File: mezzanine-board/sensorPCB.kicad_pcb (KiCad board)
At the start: 2 copper layers, 50 x 8 mm, 22 parts, among them J1 SFMC-105-01-L-D, U1 AS72651, U2 4MB Flash, U3 AS72652, U4 AS72653

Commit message: Fixed warnings
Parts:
- D1: footprint LED_SMD:LED_01005_0402Metric -> LED_SMD:LED_0603_1608Metric
- moved D1 0.68 mm to (130.9, 88.1)
- moved R6 0.64 mm to (98.9, 92.2)

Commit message: Initial Routing
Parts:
- C1, C2, C3, C4, C5, C6, C7, R4, R5, R6, R7, U2: moved to F.Cu
- moved C7 29.4 mm to (125.3, 84.6)
- moved C2 16.4 mm to (121.7, 87.0)
- moved C1 16.1 mm to (119.4, 84.6), turned to 0 degrees
- moved U2 14.7 mm to (129.9, 85.7)
- moved R7 13.8 mm to (112.6, 93.0)
- moved C5 11.8 mm to (110.2, 84.5), turned to 0 degrees
- moved C3 10.7 mm to (112.8, 86.7)
- moved R3 8.96 mm to (121.2, 92.7)
- moved R5 8.68 mm to (97.2, 84.5), turned to 0 degrees
- moved D1 8.64 mm to (123.1, 84.6)
- moved R4 8.41 mm to (116.1, 84.6), turned to 0 degrees
- moved R1 8.29 mm to (112.9, 90.0), turned to 90 degrees
- moved C6 6.35 mm to (103.8, 86.9)
- moved R2 6.06 mm to (121.7, 90.3), turned to 90 degrees
- moved R6 5.24 mm to (103.8, 90.2), turned to 90 degrees
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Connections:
- J1 pad 1: SPI_MOSI -> CSN_EE
- J1 pad 10: INT -> GND
- J1 pad 2: SPI_SCK -> RX/SCL
- J1 pad 4: RESN -> TX/SDA
- J1 pad 5: CSN_EE -> SPI_MOSI
- J1 pad 6: GND -> INT
- J1 pad 7: RX/SCL -> SPI_SCK
- J1 pad 9: TX/SDA -> RESN
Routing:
- net SPI_MOSI: track 19.2 -> 40.7 mm, vias 2 -> 1
- net +3.3V: track 106.6 -> 87.0 mm, vias 9 -> 11
- net GND: track 55.3 -> 71.2 mm, vias 5 -> 7
- net SPI_SCK: track 26.2 -> 39.8 mm
- net TX/SDA: track 20.4 -> 8.05 mm
- net I2C_ENA: track 17.2 -> 6.60 mm
- net Net-(D1-A): track 15.0 -> 5.39 mm, vias 2 -> 0
- net RESN: track 21.7 -> 30.4 mm
- net CSN_EE: track 18.2 -> 26.6 mm, vias 2 -> 1
- net SPI_MISO: track 23.1 -> 31.4 mm, vias 3 -> 1
- net RX/SCL: track 13.8 -> 6.43 mm
- net INT: track 35.4 -> 28.7 mm, vias 5 -> 3
- net /SLV1_RESN: track 25.7 -> 32.1 mm, vias 1 -> 0
- net /SCL: track 26.9 -> 29.0 mm, vias 2 -> 4
- net /SLV2_RESN: track 4.36 -> 2.49 mm, vias 1 -> 0
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- added copper zone on B.Cu, net GND
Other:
- board size 50 x 8 mm -> 50 x 12.5 mm

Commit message: Update larger board design
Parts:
- H1, H2: footprint Mounting_Wuerth:Mounting_Wuerth_WA-SMSI-M2.5_H0.5mm_9774005151 -> MountingHole:MountingHole_2.7mm_M2.5
- moved H2 0.70 mm to (136.0, 91.0)
- moved H1 0.31 mm to (92.0, 91.0)
- moved J1 0.17 mm to (124.4, 91.7)
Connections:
- U1 pad 15: Net-(D1-A) -> unconnected-(U1-LED_DRV-Pad15)
- U1 pad 18: unconnected-(U1-LED_IND-Pad18) -> Net-(D1-A)
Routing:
- net Net-(D1-A): track 5.39 -> 6.14 mm, vias 0 -> 2
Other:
- board size 50 x 12.5 mm -> 51 x 13 mm
- board text added: "DNP for I2C"

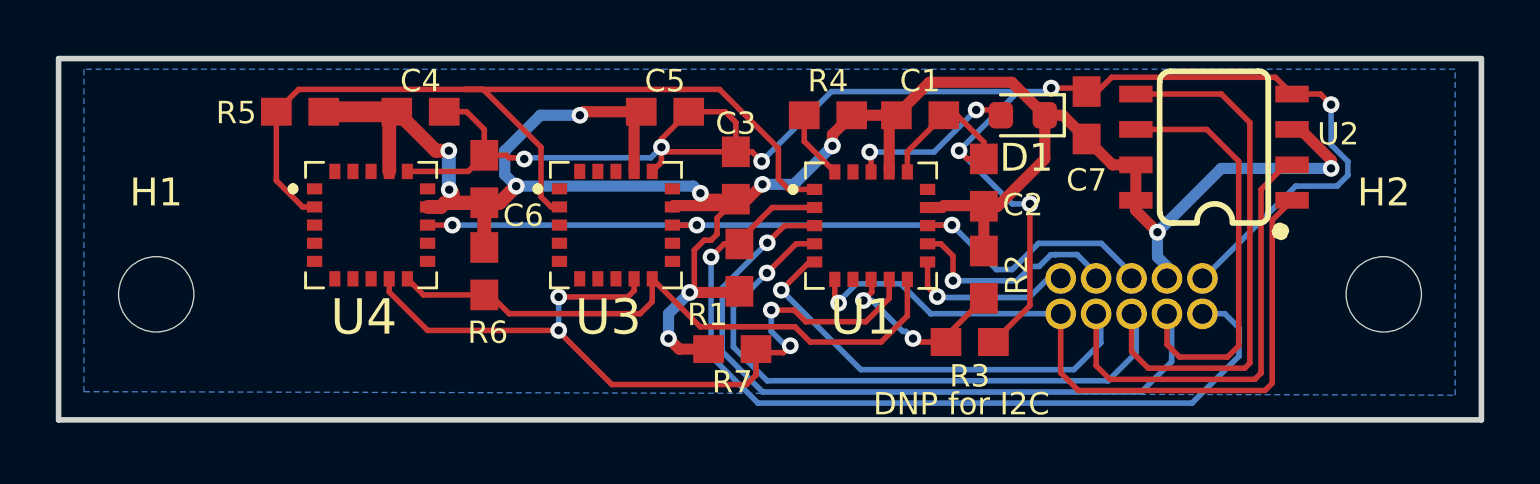
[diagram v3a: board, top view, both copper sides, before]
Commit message: Moved RA connectors back to 16mm away
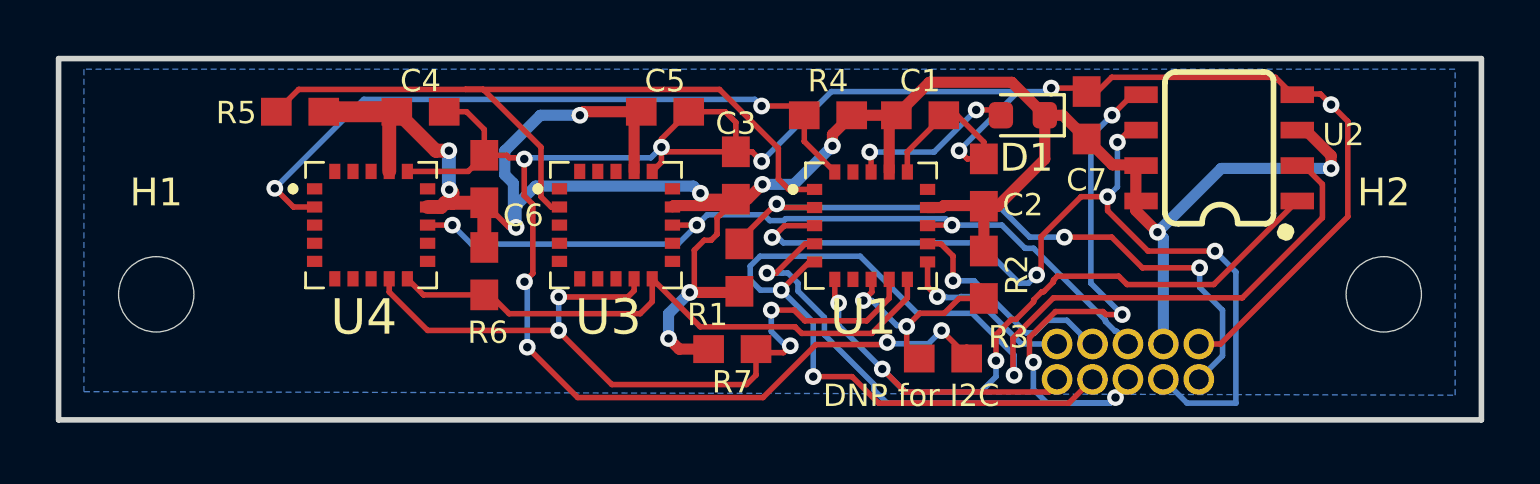
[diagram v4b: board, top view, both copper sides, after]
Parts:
- moved J1 2.35 mm to (124.3, 94.0)
- moved R3 1.13 mm to (120.2, 93.3)
- moved U2 0.19 mm to (130.1, 85.8)
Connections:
- U4 pad 2: /SLV1_RESN -> /SLV2_RESN
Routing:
- net /SLV2_RESN: track 2.49 -> 24.7 mm, vias 0 -> 2
- net GND: track 71.0 -> 89.7 mm, vias 7 -> 10
- net SPI_MISO: track 31.8 -> 46.1 mm, vias 1 -> 3
- net SPI_SCK: track 40.2 -> 33.2 mm, vias 1 -> 5
- net RESN: track 30.8 -> 24.3 mm, vias 1 -> 3
- net SPI_MOSI: track 41.1 -> 36.0 mm, vias 1 -> 5
- net /SLV1_RESN: track 32.1 -> 27.9 mm
- net CSN_EE: track 26.7 -> 30.1 mm, vias 1 -> 3
- net +3.3V: track 87.1 -> 90.4 mm
- net INT: track 28.7 -> 29.6 mm
- net I2C_ENA: track 6.60 -> 7.35 mm
- net /SDA: track 22.1 -> 21.4 mm
